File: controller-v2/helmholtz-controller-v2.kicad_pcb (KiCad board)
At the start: 2 copper layers, 72.7 x 72.1 mm, 58 parts, among them J1 Screw_Terminal_01x02, J2 Screw_Terminal_01x02, J3 Screw_Terminal_01x02, J4 Screw_Terminal_01x02, J5 Conn_01x04, U1 BDS63150AFM, U2 BDS63150AFM, U3 INA226, U4 INA226, U5 BDS63150AFM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

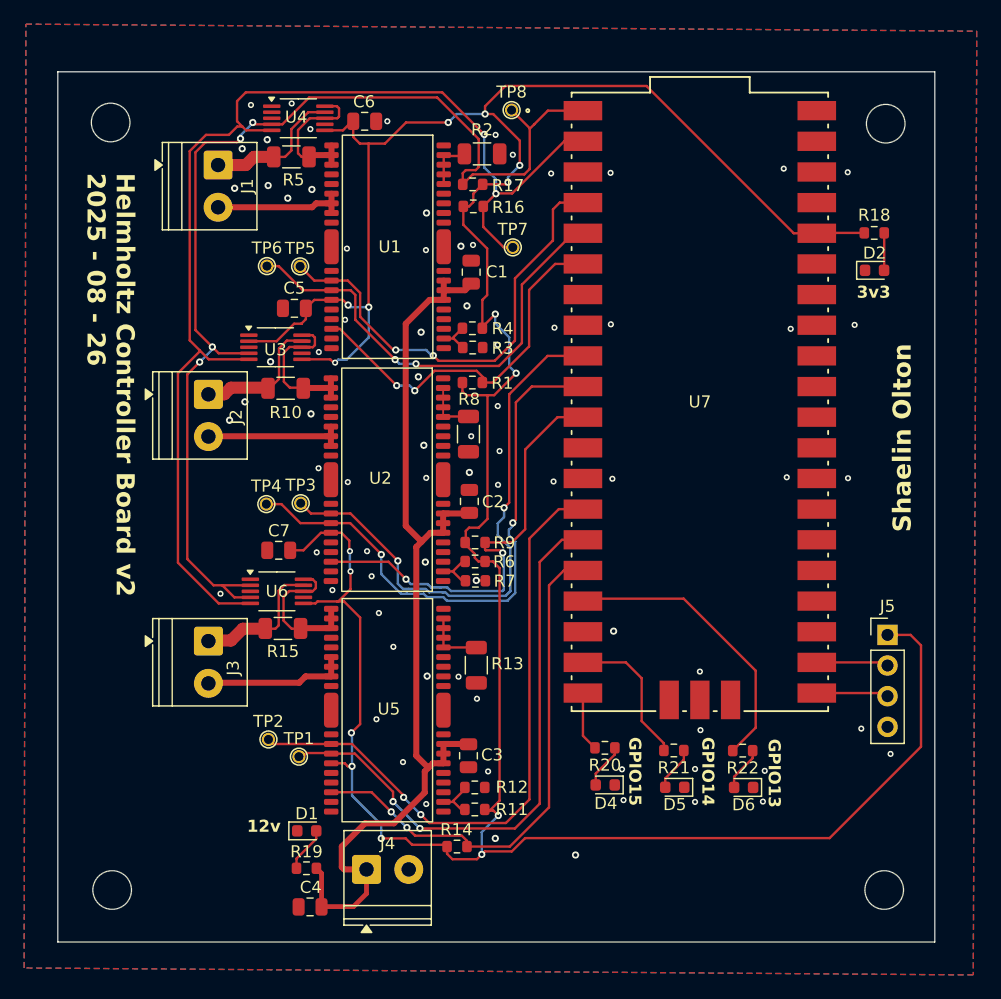
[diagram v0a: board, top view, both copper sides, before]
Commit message: Alert pins connected to pico
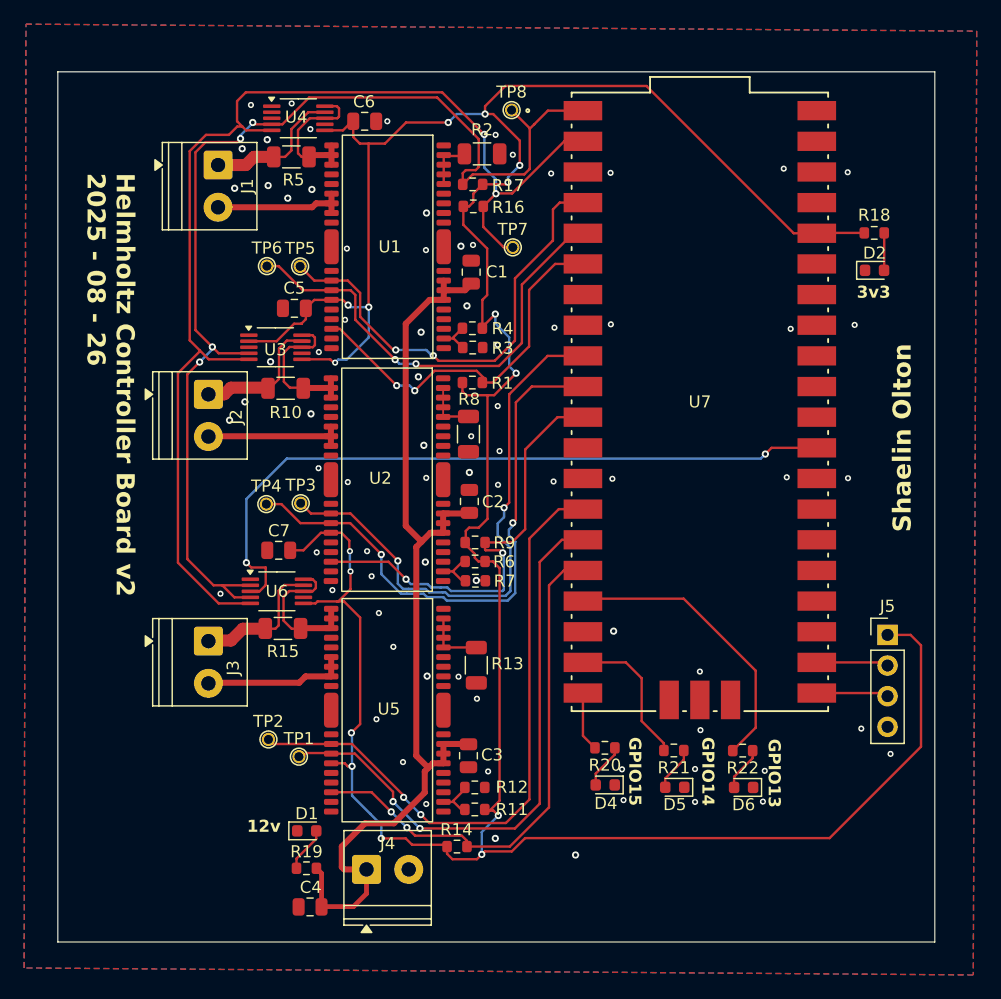
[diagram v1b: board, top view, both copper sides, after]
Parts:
- removed REF** (x4): MountingHole_3.2mm_M3, MountingHole:MountingHole_3.2mm_M3
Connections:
- U1 pad 10: (no net) -> unconnected-(U1-NC-Pad10)
- U1 pad 14: (no net) -> unconnected-(U1-NC-Pad14)
- U1 pad 17: (no net) -> unconnected-(U1-NC-Pad17)
- U1 pad 19: (no net) -> unconnected-(U1-NC-Pad19)
- U1 pad 21: (no net) -> unconnected-(U1-NC-Pad21)
- U1 pad 22: (no net) -> GND
- U1 pad 23: (no net) -> unconnected-(U1-NC-Pad23)
- U1 pad 27: (no net) -> unconnected-(U1-NC-Pad27)
- U1 pad 28: (no net) -> unconnected-(U1-NC-Pad28)
- U1 pad 30: (no net) -> unconnected-(U1-NC-Pad30)
- U1 pad 31: (no net) -> unconnected-(U1-NC-Pad31)
- U1 pad 36: (no net) -> unconnected-(U1-NC-Pad36)
- U1 pad 4: (no net) -> unconnected-(U1-NC-Pad4)
- U1 pad 5: (no net) -> unconnected-(U1-NC-Pad5)
- U1 pad 9: (no net) -> unconnected-(U1-NC-Pad9)
- U1 pad FIN: GND -> (no net)
- U2 pad 10: (no net) -> unconnected-(U2-NC-Pad10)
- U2 pad 14: (no net) -> unconnected-(U2-NC-Pad14)
- U2 pad 17: (no net) -> unconnected-(U2-NC-Pad17)
- U2 pad 19: (no net) -> unconnected-(U2-NC-Pad19)
- U2 pad 21: (no net) -> unconnected-(U2-NC-Pad21)
- U2 pad 22: (no net) -> GND
- U2 pad 23: (no net) -> unconnected-(U2-NC-Pad23)
- U2 pad 27: (no net) -> unconnected-(U2-NC-Pad27)
- U2 pad 28: (no net) -> unconnected-(U2-NC-Pad28)
- U2 pad 30: (no net) -> unconnected-(U2-NC-Pad30)
- U2 pad 31: (no net) -> unconnected-(U2-NC-Pad31)
- U2 pad 36: (no net) -> unconnected-(U2-NC-Pad36)
- U2 pad 4: (no net) -> unconnected-(U2-NC-Pad4)
- U2 pad 5: (no net) -> unconnected-(U2-NC-Pad5)
- U2 pad 9: (no net) -> unconnected-(U2-NC-Pad9)
- U2 pad FIN: GND -> (no net)
- U3 pad 3: unconnected-(U3-~{Alert}-Pad3) -> Net-(U3-~{Alert})
- U4 pad 3: unconnected-(U4-~{Alert}-Pad3) -> Net-(U4-~{Alert})
- U5 pad 10: (no net) -> unconnected-(U5-NC-Pad10)
- U5 pad 14: (no net) -> unconnected-(U5-NC-Pad14)
- U5 pad 17: (no net) -> unconnected-(U5-NC-Pad17)
- U5 pad 19: (no net) -> unconnected-(U5-NC-Pad19)
- U5 pad 21: (no net) -> unconnected-(U5-NC-Pad21)
- U5 pad 22: (no net) -> GND
- U5 pad 23: (no net) -> unconnected-(U5-NC-Pad23)
- U5 pad 27: (no net) -> unconnected-(U5-NC-Pad27)
- U5 pad 28: (no net) -> unconnected-(U5-NC-Pad28)
- U5 pad 30: (no net) -> unconnected-(U5-NC-Pad30)
- U5 pad 31: (no net) -> unconnected-(U5-NC-Pad31)
- U5 pad 36: (no net) -> unconnected-(U5-NC-Pad36)
- U5 pad 4: (no net) -> unconnected-(U5-NC-Pad4)
- U5 pad 5: (no net) -> unconnected-(U5-NC-Pad5)
- U5 pad 9: (no net) -> unconnected-(U5-NC-Pad9)
- U5 pad FIN: GND -> (no net)
- U6 pad 3: unconnected-(U6-~{Alert}-Pad3) -> Net-(U6-~{Alert})
- U7 pad 12: unconnected-(U7-GPIO9-Pad12) -> Net-(U3-~{Alert})
- U7 pad 29: unconnected-(U7-GPIO22-Pad29) -> Net-(U6-~{Alert})
- U7 pad 7: unconnected-(U7-GPIO5-Pad7) -> Net-(U4-~{Alert})
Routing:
- net Net-(U6-~{Alert}): track 0.00 -> 59.0 mm, vias 0 -> 2
